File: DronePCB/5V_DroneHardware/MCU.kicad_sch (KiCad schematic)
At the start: 20 parts, among them SW1 SW_SPDT, U1 STM32F405RGT6, Y1 16MHz

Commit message: Collegamento di USB con resistenze da 22Ohm
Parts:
- SW1: footprint Button_Switch_SMD:SW_SPDT_PCM12 -> Button_Switch_SMD:SW_SPST_B3U-1000P
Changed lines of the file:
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@@
   )
   (symbol (lib_id "Switch:SW_SPDT") (at 244.348 38.608 0) (unit 1)
-    (in_bom yes) (on_board yes) (fields_autoplaced)
-    (property "Reference" "SW1" (id 0) (at 244.348 30.988 0))
-    (property "Value" "SW_SPDT" (id 1) (at 244.348 33.528 0))
-    (property "Footprint" "Button_Switch_SMD:SW_SPDT_PCM12" (id 2) (at 244.348 38.608 0)
+    (in_bom yes) (on_board yes)
+    (property "Reference" "SW1" (id 0) (at 243.84 34.544 0))
+    (property "Value" "SW_SPDT" (id 1) (at 244.348 33.528 0)
       (effects (font (size 1.27 1.27)) hide)
     )
+    (property "Footprint" "Button_Switch_SMD:SW_SPST_B3U-1000P" (id 2) (at 244.348 38.608 0)
+      (effects (font (size 1.27 1.27)) hide)
+    )

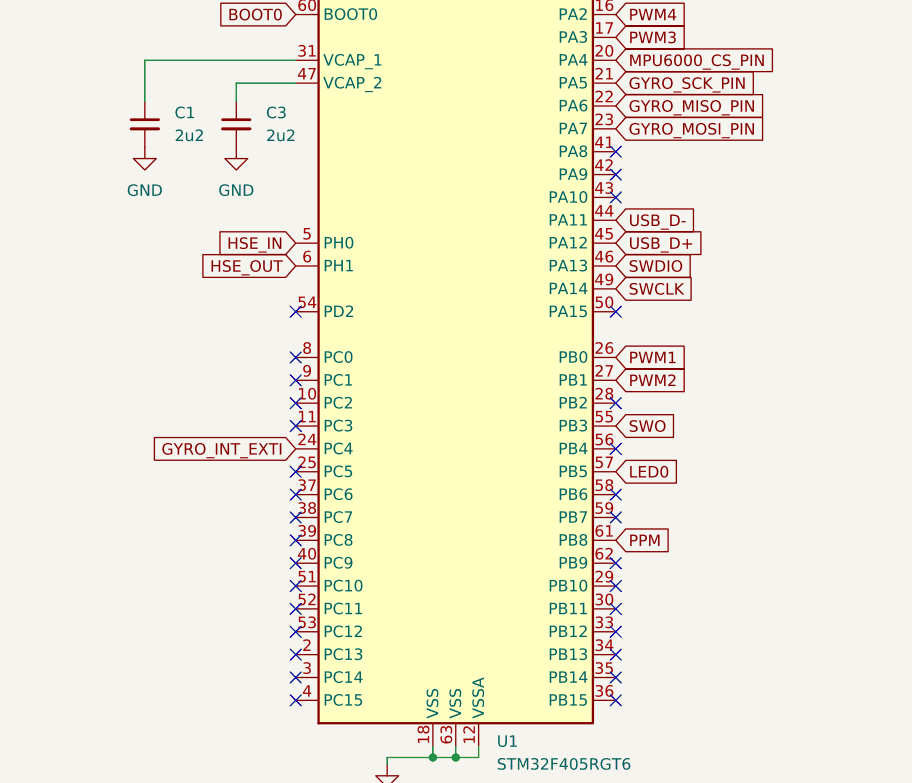
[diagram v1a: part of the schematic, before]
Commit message: Aggiunta di USART per RC
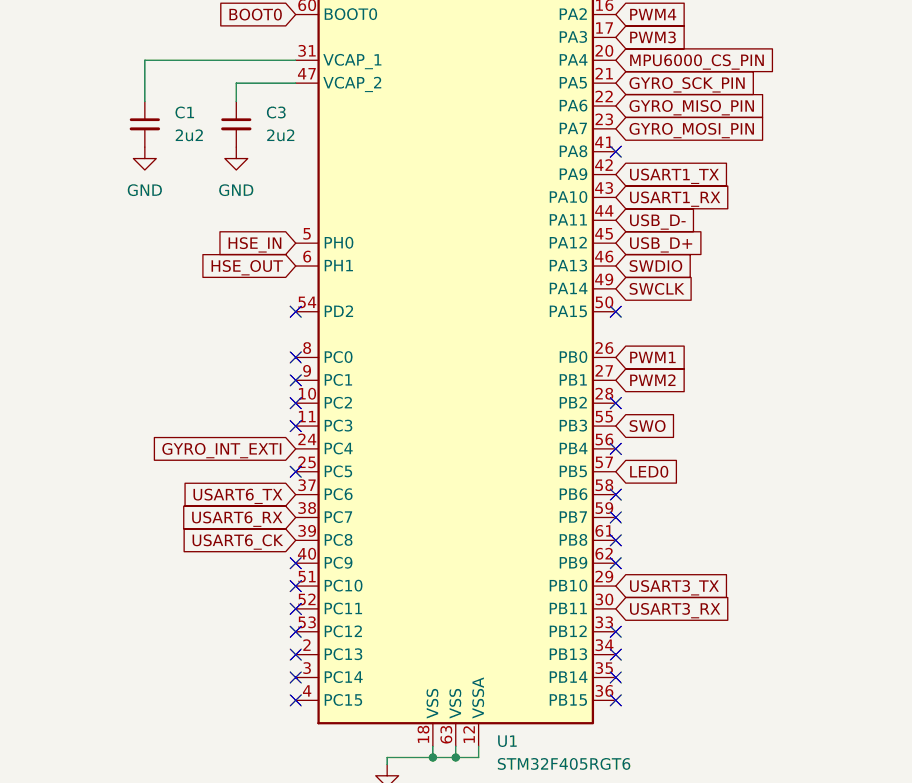
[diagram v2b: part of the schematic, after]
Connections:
- net USART3_TX: now reaches U1.29 (PB10)
- net USART3_RX: now reaches U1.30 (PB11)
- net USART6_TX: now reaches U1.37 (PC6)
- net USART6_RX: now reaches U1.38 (PC7)
- net USART6_CK: now reaches U1.39 (PC8)
- net USART1_TX: now reaches U1.42 (PA9)
- net USART1_RX: now reaches U1.43 (PA10)
- net PPM: no longer names the net of U1.61 (PB8)
- no-connect marks 33 -> 27
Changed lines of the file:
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@@
   (junction (at 144.018 65.024) (diameter 0) (color 0 0 0 0)
   )
-  (no_connect (at 156.718 96.52))
   (no_connect (at 156.718 91.44))
-  (no_connect (at 121.158 132.08))
-  (no_connect (at 156.718 93.98))
   (no_connect (at 156.718 129.54))
   (no_connect (at 156.718 73.66))
@@
   (no_connect (at 156.718 149.86))
   (no_connect (at 121.158 119.38))
-  (no_connect (at 156.718 139.7))
   (no_connect (at 121.158 121.92))
   (no_connect (at 156.718 71.12))
@@
   (no_connect (at 156.718 137.16))
   (no_connect (at 156.718 144.78))
-  (no_connect (at 121.158 129.54))
   (no_connect (at 156.718 109.22))
   (no_connect (at 121.158 109.22))
-  (no_connect (at 156.718 142.24))
   (no_connect (at 156.718 147.32))
   (no_connect (at 121.158 137.16))
-  (no_connect (at 121.158 134.62))
+  (no_connect (at 156.718 134.62))
   (wire (pts (xy 138.938 65.024) (xy 141.478 65.024))
     (stroke (width 0) (type default) (color 0 0 0 0))
@@
     )
   )
+  (global_label "USART1_TX" (shape input) (at 156.718 93.98 0) (fields_autoplaced)
+    (effects (font (size 1.27 1.27)) (justify left))
+    (property "Intersheet References" "${INTERSHEET_REFS}" (id 0) (at 169.3516 93.9006 0)
+      (effects (font (size 1.27 1.27)) (justify left) hide)
+    )
+  )
+  (global_label "USART6_CK" (shape input) (at 121.158 134.62 180) (fields_autoplaced)
+    (effects (font (size 1.27 1.27)) (justify right))
+    (property "Intersheet References" "${INTERSHEET_REFS}" (id 0) (at 108.1616 134.5406 0)
+      (effects (font (size 1.27 1.27)) (justify right) hide)
+    )
+  )
   (global_label "USB_D-" (shape input) (at 156.718 99.06 0) (fields_autoplaced)
     (effects (font (size 1.27 1.27)) (justify left))
@@
     )
   )
+  (global_label "USART3_TX" (shape input) (at 156.718 139.7 0) (fields_autoplaced)
+    (effects (font (size 1.27 1.27)) (justify left))
+    (property "Intersheet References" "${INTERSHEET_REFS}" (id 0) (at 169.3516 139.6206 0)
+      (effects (font (size 1.27 1.27)) (justify left) hide)
+    )
+  )
   (global_label "HSE_OUT" (shape input) (at 121.158 104.14 180) (fields_autoplaced)
     (effects (font (size 1.27 1.27)) (justify right))
@@
     )
   )
+  (global_label "USART1_RX" (shape input) (at 156.718 96.52 0) (fields_autoplaced)
+    (effects (font (size 1.27 1.27)) (justify left))
+    (property "Intersheet References" "${INTERSHEET_REFS}" (id 0) (at 169.654 96.4406 0)
+      (effects (font (size 1.27 1.27)) (justify left) hide)
+    )
+  )
   (global_label "HSE_IN" (shape input) (at 121.158 101.6 180) (fields_autoplaced)
     (effects (font (size 1.27 1.27)) (justify right))
@@
     )
   )
+  (global_label "USART6_RX" (shape input) (at 121.158 132.08 180) (fields_autoplaced)
+    (effects (font (size 1.27 1.27)) (justify right))
+    (property "Intersheet References" "${INTERSHEET_REFS}" (id 0) (at 108.222 132.1594 0)
+      (effects (font (size 1.27 1.27)) (justify right) hide)
+    )
+  )
   (global_label "PWM4" (shape input) (at 156.718 76.2 0) (fields_autoplaced)
     (effects (font (size 1.27 1.27)) (justify left))
@@
     )
   )
+  (global_label "USART3_RX" (shape input) (at 156.718 142.24 0) (fields_autoplaced)
+    (effects (font (size 1.27 1.27)) (justify left))
+    (property "Intersheet References" "${INTERSHEET_REFS}" (id 0) (at 169.654 142.1606 0)
+      (effects (font (size 1.27 1.27)) (justify left) hide)
+    )
+  )
   (global_label "HSE_OUT" (shape input) (at 257.302 85.09 0) (fields_autoplaced)
     (effects (font (size 1.27 1.27)) (justify left))
@@
     )
   )
+  (global_label "USART6_TX" (shape input) (at 121.158 129.54 180) (fields_autoplaced)
+    (effects (font (size 1.27 1.27)) (justify right))
+    (property "Intersheet References" "${INTERSHEET_REFS}" (id 0) (at 108.5244 129.6194 0)
+      (effects (font (size 1.27 1.27)) (justify right) hide)
+    )
+  )
   (global_label "LED0" (shape input) (at 156.718 127 0) (fields_autoplaced)
     (effects (font (size 1.27 1.27)) (justify left))
@@
       (effects (font (size 1.27 1.27)) (justify left) hide)
     )
-  )
-  (global_label "PPM" (shape input) (at 156.718 134.62 0) (fields_autoplaced)
-    (effects (font (size 1.27 1.27)) (justify left))
-    (property "Intersheet References" "${INTERSHEET_REFS}" (id 0) (at 163.1225 134.5406 0)
-      (effects (font (size 1.27 1.27)) (justify left) hide)
-    )

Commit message: BOM e pos file
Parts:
- U1: LCSC Part # (none) -> C15742
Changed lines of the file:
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@@
+      (effects (font (size 1.27 1.27)) hide)
+    )
+    (property "LCSC Part #" "C15742" (id 4) (at 138.938 111.76 0)
       (effects (font (size 1.27 1.27)) hide)
     )
